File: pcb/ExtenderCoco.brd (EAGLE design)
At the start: 73.7 x 99.1 mm, 12 parts, among them X1 EXPANSION_PORT_COCO, X2 EXPANSION_PORT_COCOS, X3 EXPANSION_PORT_COCOM

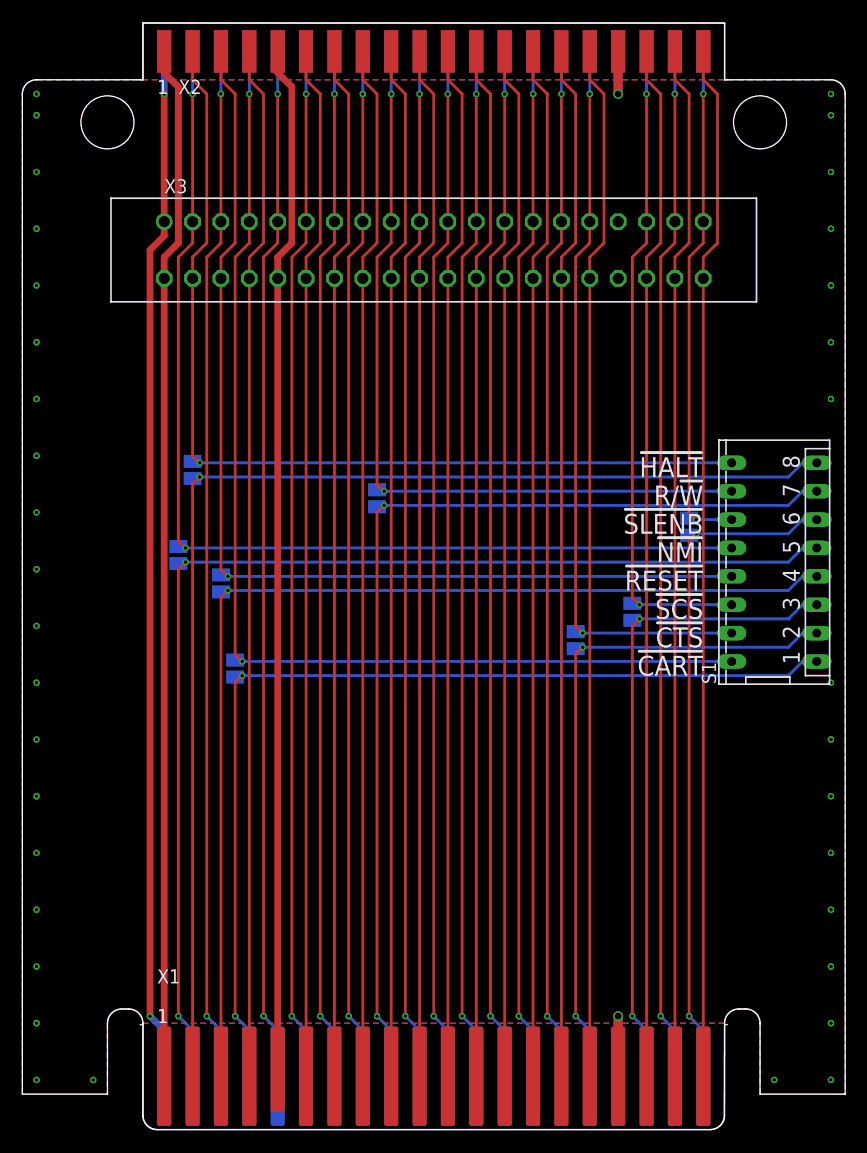
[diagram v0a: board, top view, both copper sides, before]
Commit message: Cart port connector was too narrow...
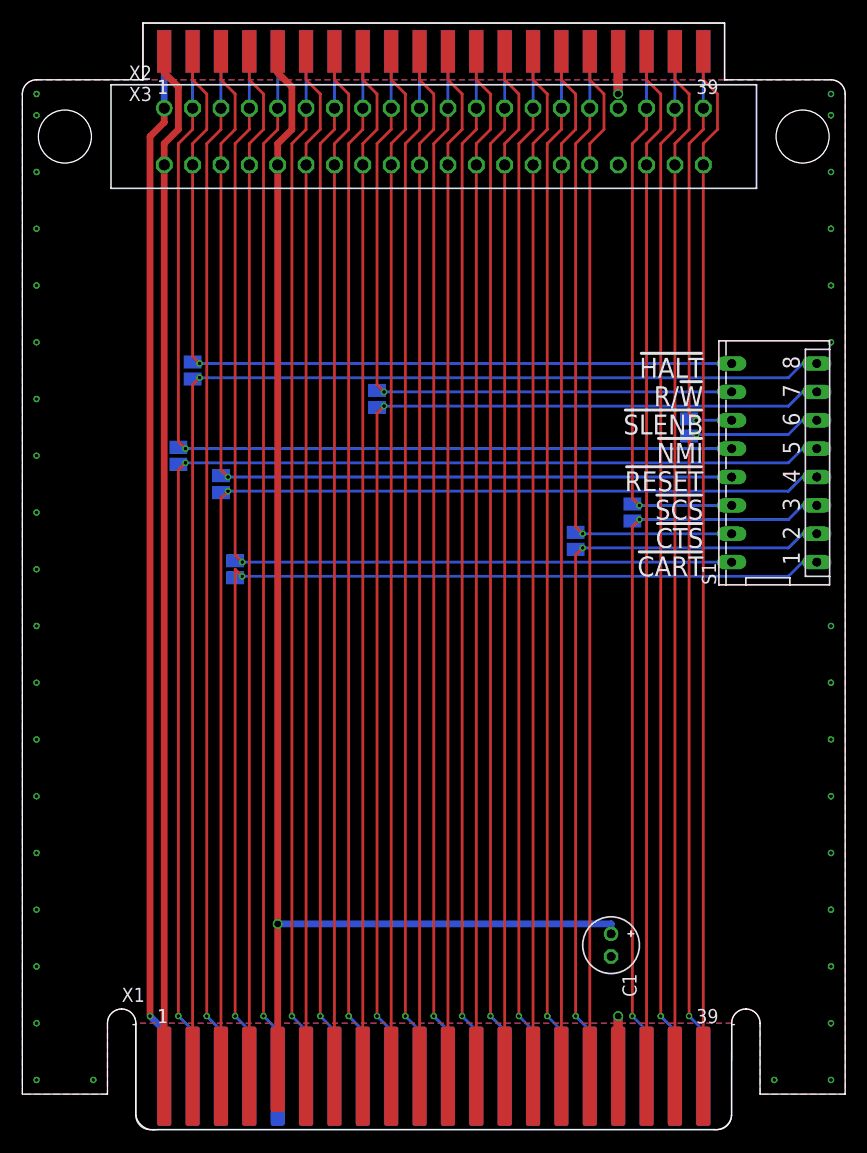
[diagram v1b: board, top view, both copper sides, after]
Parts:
- added C1: (no value), rcl:E2-5
- X2: value EXPANSION_PORT_COCOS -> EXPANSION_PORT_COCOM; device coco:MA20-2_SHORT -> coco:FE20-2
- X3: value EXPANSION_PORT_COCOM -> EXPANSION_PORT_COCOS; device coco:FE20-2 -> coco:MA20-2_SHORT
- moved X3 17.8 mm to (0.00, 96.5)
- moved S1 8.89 mm to (30.5, 59.7)
- moved SJ1 8.89 mm to (-17.8, 50.2)
- moved SJ2 8.89 mm to (12.7, 52.7)
- moved SJ3 8.89 mm to (17.8, 55.2)
- moved SJ5 8.89 mm to (-22.9, 60.3)
- moved SJ6 8.89 mm to (22.9, 62.9)
- moved SJ7 8.89 mm to (-5.08, 65.4)
- moved SJ4 8.89 mm to (-19.1, 57.8)
- moved SJ8 8.89 mm to (-21.6, 67.9)
- moved X2 7.62 mm to (0.00, 88.9)
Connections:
- net GND: now also C1.-
- net VCC: now also C1.+
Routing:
- net VCC: track 92.2 -> 122.9 mm, vias 0 -> 1
- net !CART: track 89.3 -> 99.5 mm
- net R/!W: track 91.8 -> 100.7 mm
- net !SLENB': track 46.6 -> 37.7 mm, vias 2 -> 1
- net !RESET': track 94.1 -> 85.2 mm
- net !HALT': track 86.5 -> 77.6 mm
- net !CART': track 99.9 -> 91.0 mm, vias 2 -> 1
- net R/!W': track 72.0 -> 63.1 mm, vias 2 -> 1
- net !SCS': track 59.3 -> 50.4 mm, vias 2 -> 1
- net !NMI': track 94.8 -> 85.9 mm, vias 2 -> 1
- net !CTS': track 66.9 -> 58.0 mm, vias 2 -> 1
- net !SLENB: track 61.4 -> 70.3 mm
- net !SCS: track 58.8 -> 67.7 mm
- net !RESET: track 97.7 -> 106.6 mm
- net !NMI: track 104.5 -> 113.4 mm
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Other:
- outline, holes or cut-outs redrawn
